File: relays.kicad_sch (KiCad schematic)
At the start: 0 parts

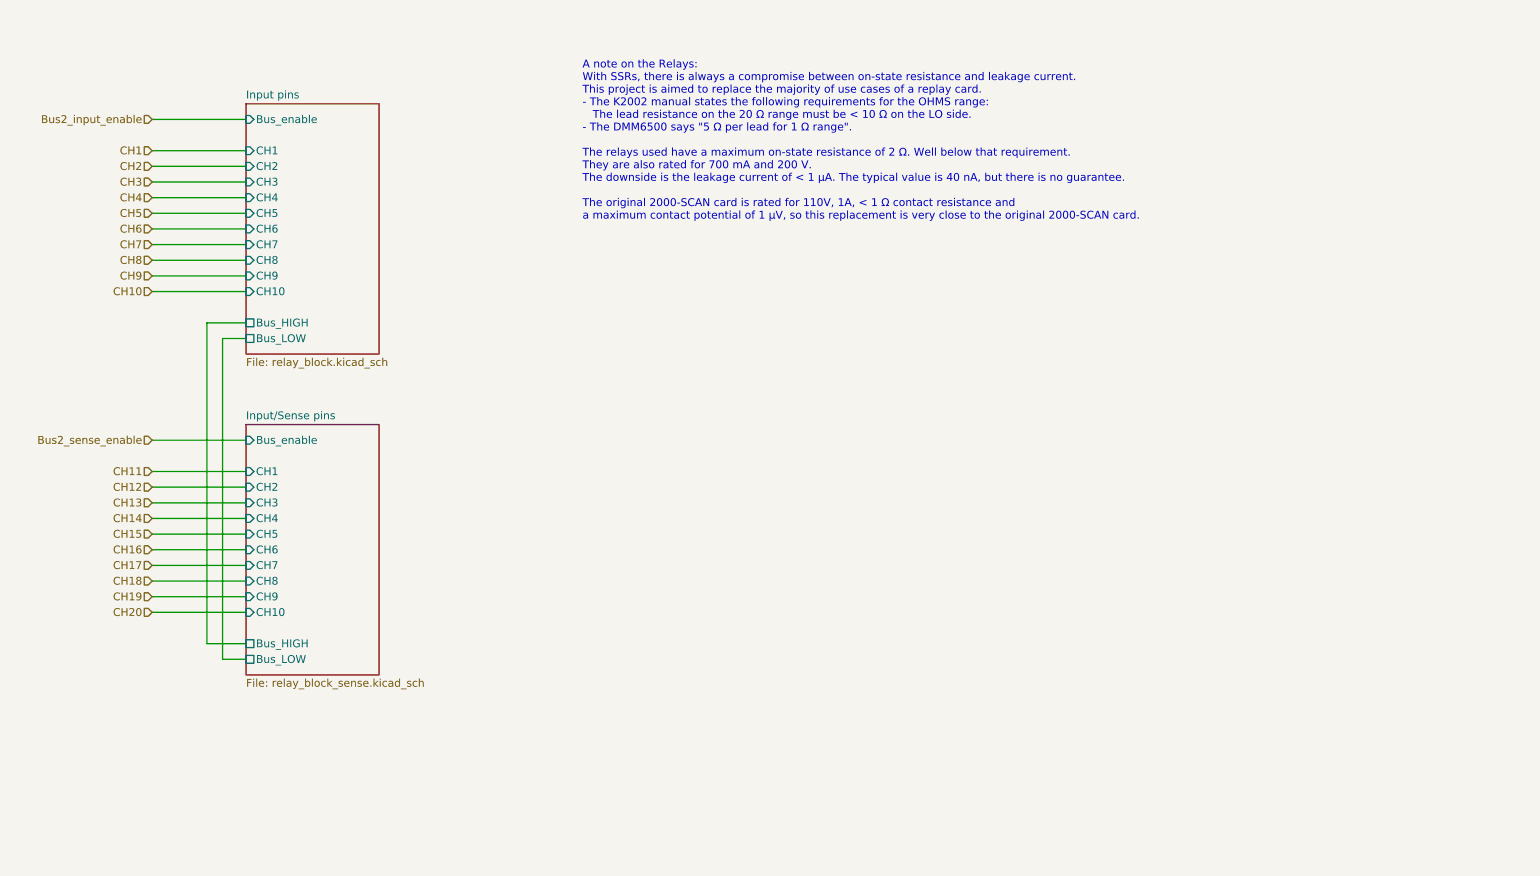
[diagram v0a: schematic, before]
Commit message: Replace the STM32 with an iCE40 FPGA (#3)
* Replaced the STM32 microcontroller with an iCE40 FPGA

* Bump version to 2.0.2, because of the update to KiCad 8

* Updated BOM properties

* Updated PCB image

* Updated readme for the FPGA version

* Updated links
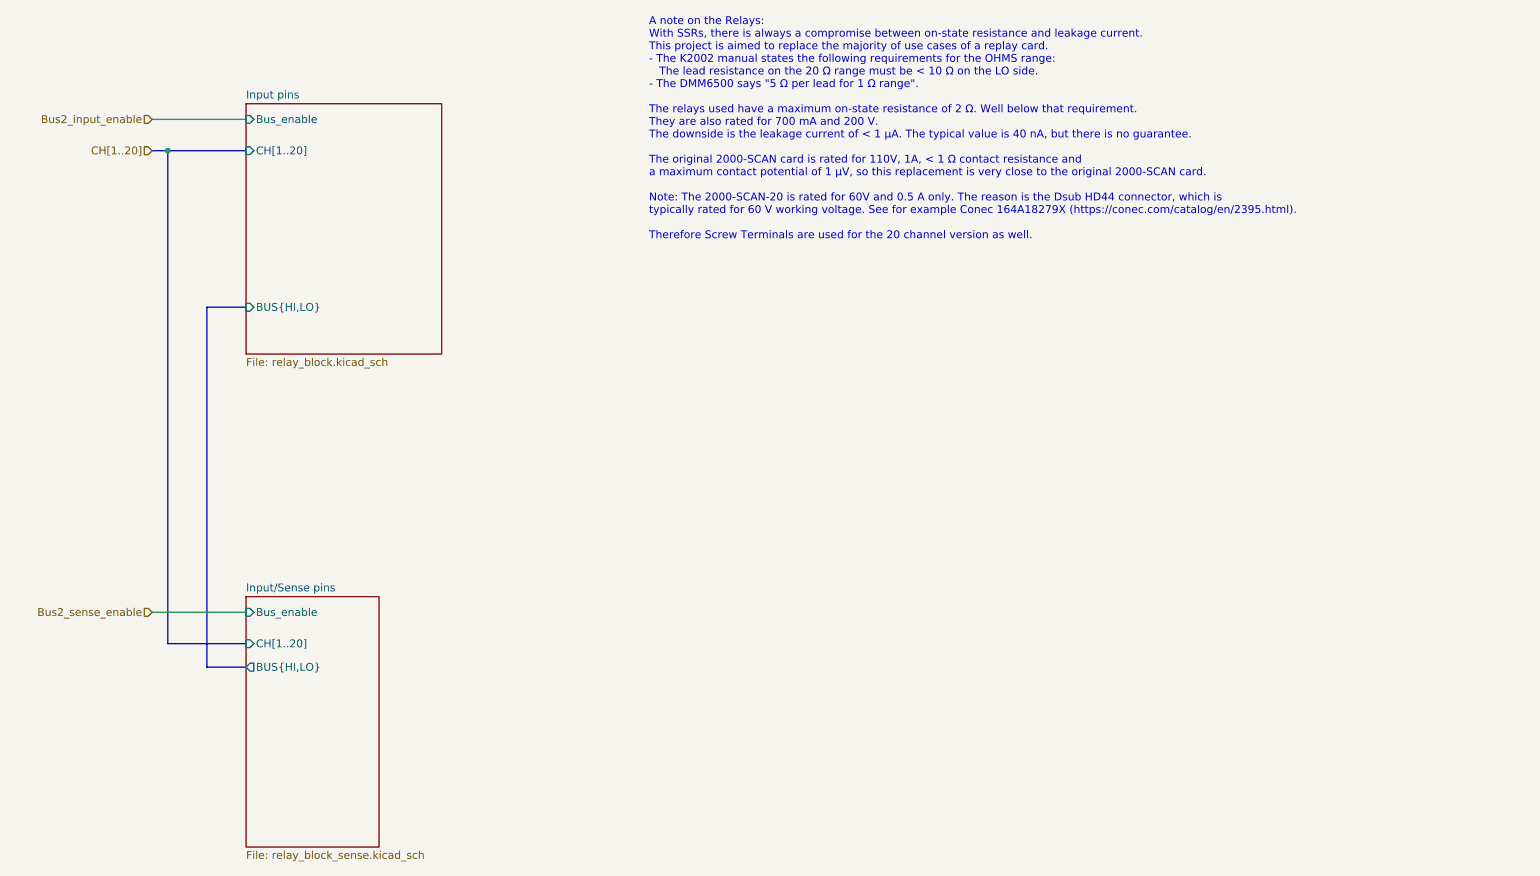
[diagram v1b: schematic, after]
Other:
- sheet Input pins ports: added BUS{HI,LO}, CH[1..20]; removed Bus_HIGH, Bus_LOW, CH1, CH10, CH2, CH3, CH4, CH5, CH6, CH7, CH8, CH9
- sheet Input/Sense pins ports: added BUS{HI,LO}, CH[1..20]; removed Bus_HIGH, Bus_LOW, CH1, CH10, CH2, CH3, CH4, CH5, CH6, CH7, CH8, CH9
